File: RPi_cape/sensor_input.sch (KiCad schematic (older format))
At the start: 39 parts, among them U5 LM2903, U6 LMC7101B, U7 LMC7101B

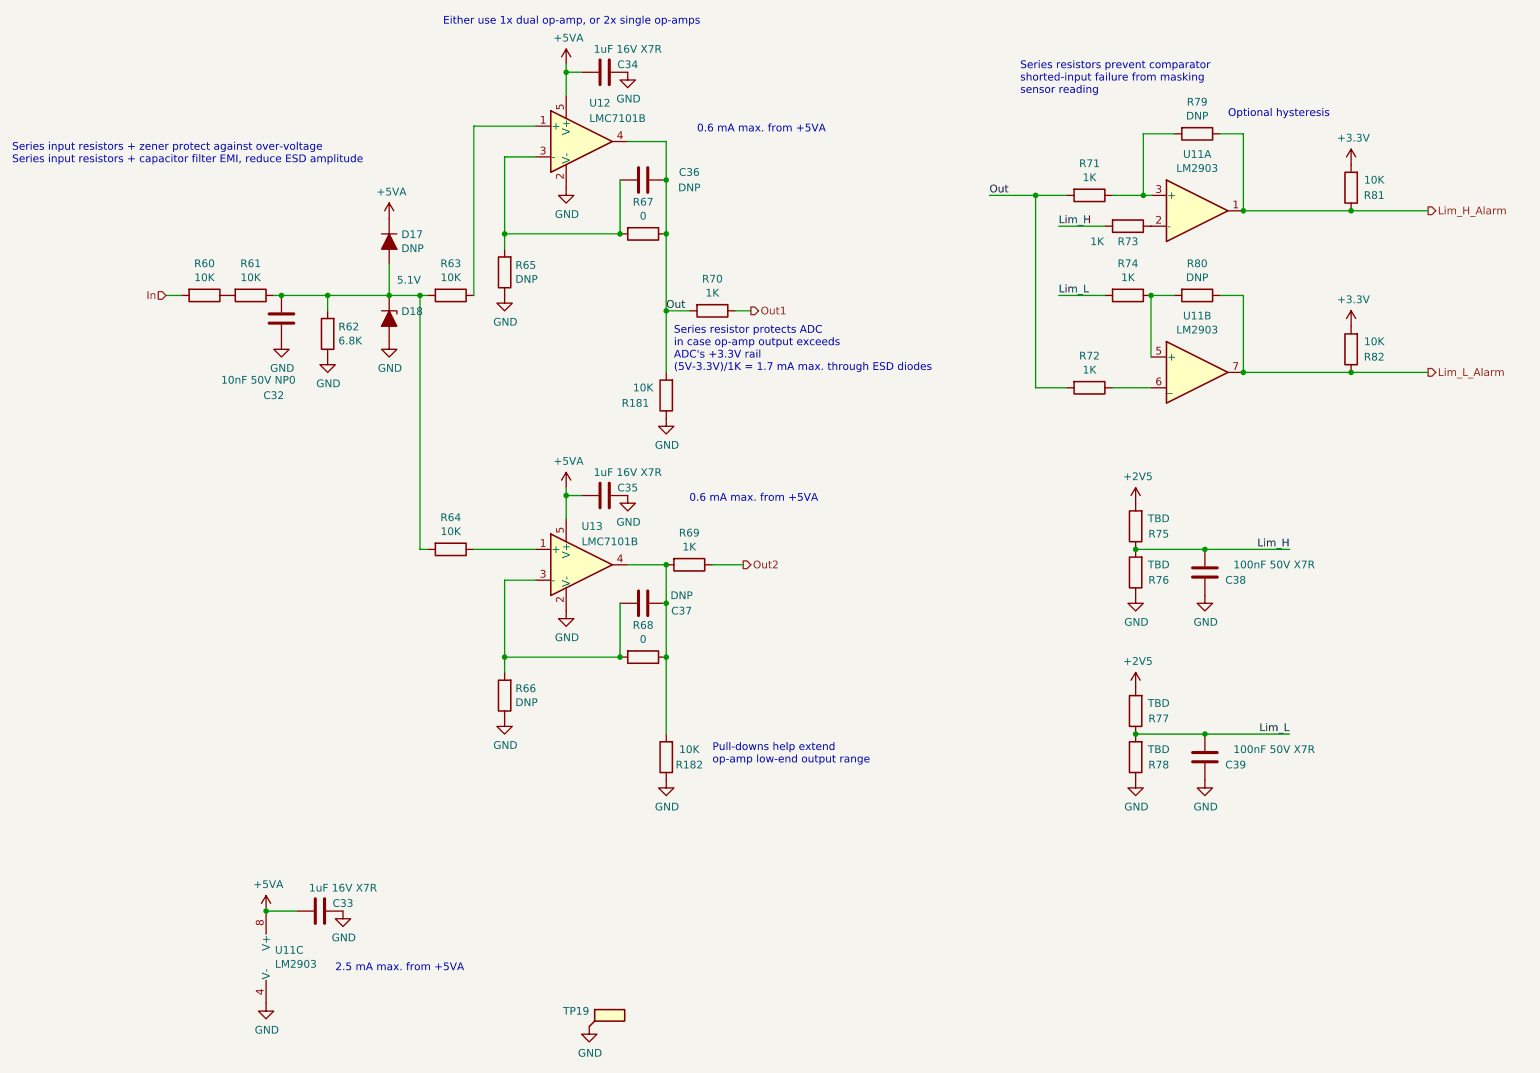
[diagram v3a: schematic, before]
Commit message: Better valve monitoring, finalized layout and manufacturing files
Created assembly and fabrication drawings, assigned all BOM parts, generally made design ready for ordering
Added strain-relief slots and barb mounting dimensions for digital pressure sensors
Changed valve drivers from discrete power MOSFETs to "smart" industrial/automotive driver ICs for the current monitoring, including valve-movement monitor for #4
Connected RPi_Valve* signals to larger CPLD footprint, changed Raspberry Pi pin assignment as a result to ease PCB routing
Updated footprints, page layout to create readable assembly drawing
Added current-measurement testpoints for CPLD power from BATT+
Changed power diodes in power-down-alarm circuit to small-signal parts for more compact layout
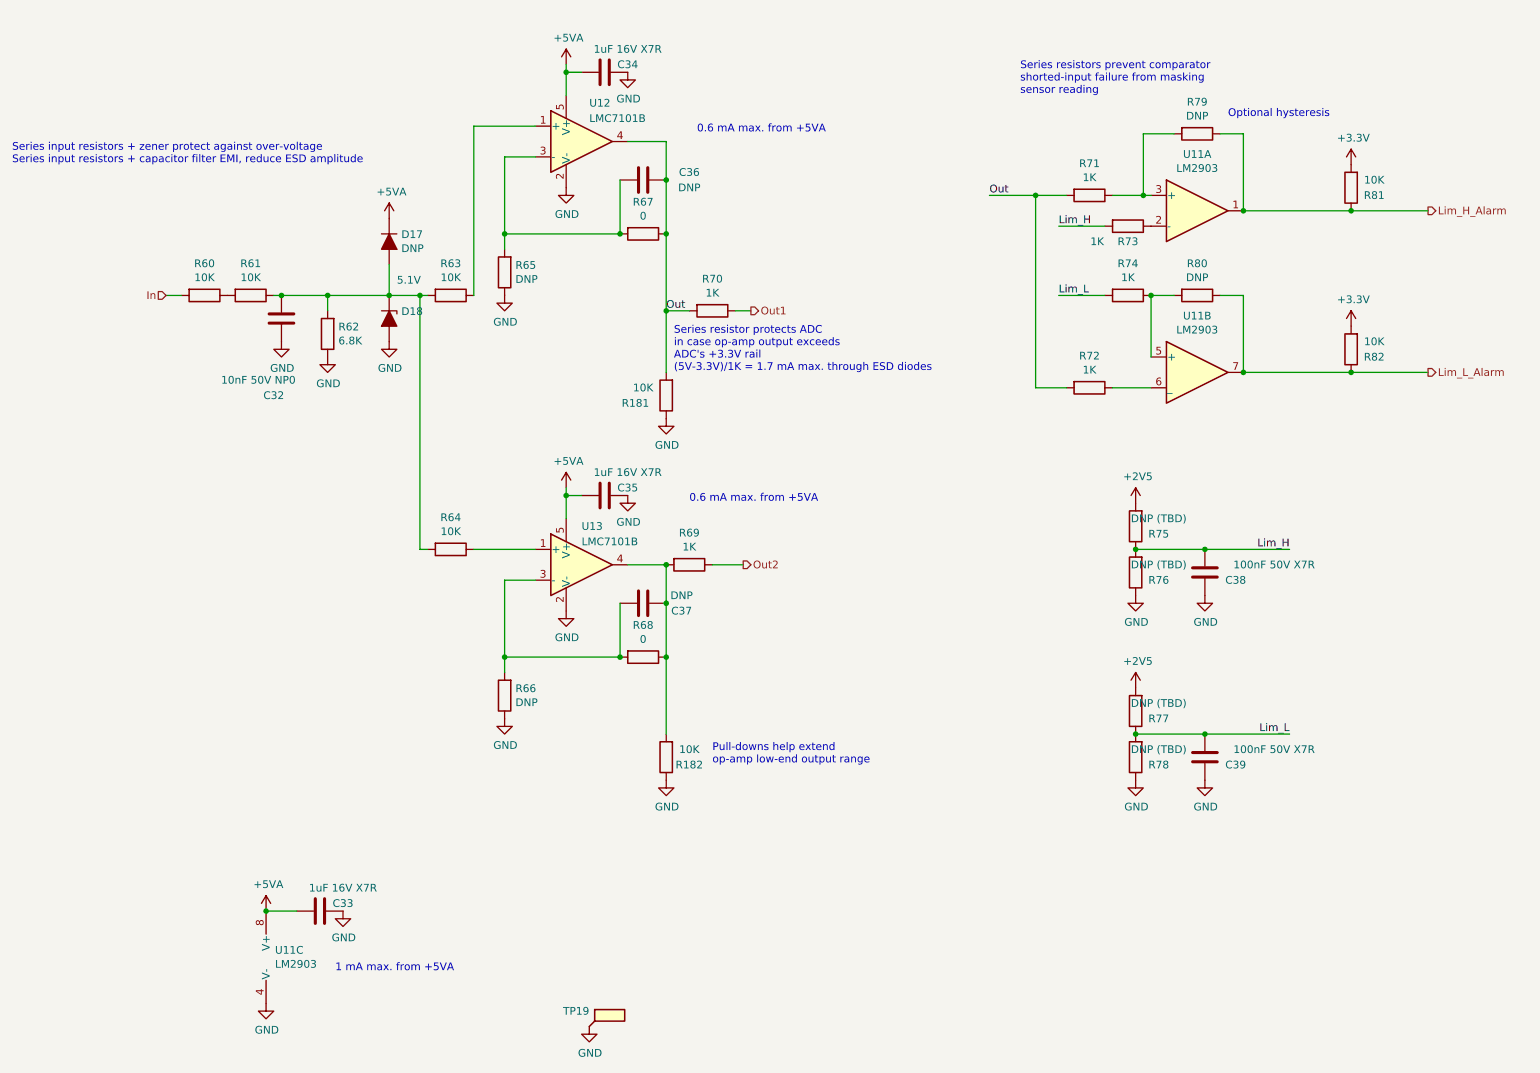
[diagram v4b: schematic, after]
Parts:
- D10: footprint Diode_SMD:D_SOD-123 -> Ventilator:D_SOD-123
- D11: footprint Diode_SMD:D_SOD-123 -> Ventilator:D_SOD-123; Manufacturer (none) -> ON Semiconductor; Part Number (none) -> MMSZ5231BT1G
- R179, R180, R30, R31, R33, R34, R51, R52: Manufacturer (none) -> KOA Speer; Part Number (none) -> RK73H2BTTD1002F
- R32: Manufacturer (none) -> KOA Speer; Part Number (none) -> RK73H2BTTD6801F
- R37, R38: Manufacturer (none) -> Panasonic; Part Number (none) -> ERJ-8GEY0R00V
- R39, R40, R41, R42, R43, R44: Manufacturer (none) -> KOA Speer; Part Number (none) -> RK73H2BTTD1001F
- R45, R46, R47, R48: value TBD -> DNP (TBD)
- U5: footprint Package_SO:VSSOP-8_3.0x3.0mm_P0.65mm -> Ventilator:VSSOP-8_3.0x3.0mm_P0.65mm
- U6, U7: footprint Package_TO_SOT_SMD:SOT-23-5 -> Ventilator:SOT-23-5
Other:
- note added: "1 mA max. from +5VA"
- note removed: "2.5 mA max. from +5VA"
- note removed: "Either use 1x dual op-amp, or 2x single op-amps"
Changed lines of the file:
@@
 $Descr A4 11693 8268
 encoding utf-8
-Sheet 4 14
+Sheet 4 15
 Title "Sensor Input (0-10V)"
 Date ""
@@
 F 2 "Resistor_SMD:R_1206_3216Metric" V 3380 4300 50  0001 C CNN
 F 3 "~" H 3450 4300 50  0001 C CNN
+F 4 "KOA Speer" H 3450 4300 50  0001 C CNN "Manufacturer"
+F 5 "RK73H2BTTD1002F" H 3450 4300 50  0001 C CNN "Part Number"
 	1    3450 4300
 	0    1    1    0
@@
 F 2 "Resistor_SMD:R_1206_3216Metric" V 4630 5000 50  0001 C CNN
 F 3 "~" H 4700 5000 50  0001 C CNN
+F 4 "Panasonic" H 4700 5000 50  0001 C CNN "Manufacturer"
+F 5 "ERJ-8GEY0R00V" H 4700 5000 50  0001 C CNN "Part Number"
 	1    4700 5000
 	0    1    1    0
@@
 F 0 "D18" V 3004 2879 50  0000 L CNN
 F 1 "5.1V" V 2800 2850 50  0000 L CNN
-F 2 "Diode_SMD:D_SOD-123" H 3050 2800 50  0001 C CNN
+F 2 "Ventilator:D_SOD-123" H 3050 2800 50  0001 C CNN
 F 3 "~" H 3050 2800 50  0001 C CNN
+F 4 "ON Semiconductor" H 3050 2800 50  0001 C CNN "Manufacturer"
+F 5 "MMSZ5231BT1G" H 3050 2800 50  0001 C CNN "Part Number"
 	1    3050 2800
 	0    1    1    0
@@
 F 2 "Resistor_SMD:R_1206_3216Metric" V 2580 2900 50  0001 C CNN
 F 3 "~" H 2650 2900 50  0001 C CNN
+F 4 "KOA Speer" H 2650 2900 50  0001 C CNN "Manufacturer"
+F 5 "RK73H2BTTD6801F" H 2650 2900 50  0001 C CNN "Part Number"
 	1    2650 2900
 	-1   0    0    1
@@
 F 2 "Resistor_SMD:R_1206_3216Metric" V 3380 2650 50  0001 C CNN
 F 3 "~" H 3450 2650 50  0001 C CNN
+F 4 "KOA Speer" H 3450 2650 50  0001 C CNN "Manufacturer"
+F 5 "RK73H2BTTD1002F" H 3450 2650 50  0001 C CNN "Part Number"
 	1    3450 2650
 	0    1    1    0
@@
 F 2 "Resistor_SMD:R_1206_3216Metric" V 1780 2650 50  0001 C CNN
 F 3 "~" H 1850 2650 50  0001 C CNN
+F 4 "KOA Speer" H 1850 2650 50  0001 C CNN "Manufacturer"
+F 5 "RK73H2BTTD1002F" H 1850 2650 50  0001 C CNN "Part Number"
 	1    1850 2650
 	0    1    1    0
@@
 F 2 "Resistor_SMD:R_1206_3216Metric" V 2080 2650 50  0001 C CNN
 F 3 "~" H 2150 2650 50  0001 C CNN
+F 4 "KOA Speer" H 2150 2650 50  0001 C CNN "Manufacturer"
+F 5 "RK73H2BTTD1002F" H 2150 2650 50  0001 C CNN "Part Number"
 	1    2150 2650
 	0    1    1    0
@@
 F 2 "Resistor_SMD:R_1206_3216Metric" V 4630 2250 50  0001 C CNN
 F 3 "~" H 4700 2250 50  0001 C CNN
+F 4 "Panasonic" H 4700 2250 50  0001 C CNN "Manufacturer"
+F 5 "ERJ-8GEY0R00V" H 4700 2250 50  0001 C CNN "Part Number"
 	1    4700 2250
 	0    1    1    0
@@
 F 0 "U13" H 4300 4650 50  0000 L CNN
 F 1 "LMC7101B" H 4300 4550 50  0000 L CNN
-F 2 "Package_TO_SOT_SMD:SOT-23-5" H 4300 4400 50  0001 L CNN
+F 2 "Ventilator:SOT-23-5" H 4300 4400 50  0001 L CNN
 F 3 "" H 4300 4400 50  0001 C CNN
 F 4 "Texas Instruments" H 4300 4400 50  0001 C CNN "Manufacturer"
@@
 F 0 "U12" H 4350 1900 50  0000 L CNN
 F 1 "LMC7101B" H 4350 1800 50  0000 L CNN
-F 2 "Package_TO_SOT_SMD:SOT-23-5" H 4300 1650 50  0001 L CNN
+F 2 "Ventilator:SOT-23-5" H 4300 1650 50  0001 L CNN
 F 3 "" H 4300 1650 50  0001 C CNN
 F 4 "Texas Instruments" H 4300 1650 50  0001 C CNN "Manufacturer"
@@
 F 2 "Resistor_SMD:R_1206_3216Metric" V 4930 4400 50  0001 C CNN
 F 3 "~" H 5000 4400 50  0001 C CNN
+F 4 "KOA Speer" H 5000 4400 50  0001 C CNN "Manufacturer"
+F 5 "RK73H2BTTD1001F" H 5000 4400 50  0001 C CNN "Part Number"
 	1    5000 4400
 	0    1    1    0
@@
 F 0 "D17" V 3004 2379 50  0000 L CNN
 F 1 "DNP" V 3095 2379 50  0000 L CNN
-F 2 "Diode_SMD:D_SOD-123" H 3050 2300 50  0001 C CNN
+F 2 "Ventilator:D_SOD-123" H 3050 2300 50  0001 C CNN
 F 3 "~" H 3050 2300 50  0001 C CNN
 	1    3050 2300
@@
 F 0 "U11" H 8300 2467 50  0000 C CNN
 F 1 "LM2903" H 8300 2376 50  0000 C CNN
-F 2 "Package_SO:VSSOP-8_3.0x3.0mm_P0.65mm" H 8300 2100 50  0001 C CNN
+F 2 "Ventilator:VSSOP-8_3.0x3.0mm_P0.65mm" H 8300 2100 50  0001 C CNN
 F 3 "http://www.ti.com/lit/ds/symlink/lm393-n.pdf" H 8300 2100 50  0001 C CNN
 F 4 "Texas Instruments" H 8300 2100 50  0001 C CNN "Manufacturer"
@@
 F 0 "U11" H 8300 3517 50  0000 C CNN
 F 1 "LM2903" H 8300 3426 50  0000 C CNN
-F 2 "Package_SO:VSSOP-8_3.0x3.0mm_P0.65mm" H 8300 3150 50  0001 C CNN
+F 2 "Ventilator:VSSOP-8_3.0x3.0mm_P0.65mm" H 8300 3150 50  0001 C CNN
 F 3 "http://www.ti.com/lit/ds/symlink/lm393-n.pdf" H 8300 3150 50  0001 C CNN
 F 4 "Texas Instruments" H 8300 3150 50  0001 C CNN "Manufacturer"
@@
 F 0 "U11" H 2308 6996 50  0000 L CNN
 F 1 "LM2903" H 2308 6905 50  0000 L CNN
-F 2 "Package_SO:VSSOP-8_3.0x3.0mm_P0.65mm" H 2350 6950 50  0001 C CNN
+F 2 "Ventilator:VSSOP-8_3.0x3.0mm_P0.65mm" H 2350 6950 50  0001 C CNN
 F 3 "http://www.ti.com/lit/ds/symlink/lm393-n.pdf" H 2350 6950 50  0001 C CNN
 F 4 "Texas Instruments" H 2350 6950 50  0001 C CNN "Manufacturer"
@@
 F 2 "Resistor_SMD:R_1206_3216Metric" V 5080 2750 50  0001 C CNN
 F 3 "~" H 5150 2750 50  0001 C CNN
+F 4 "KOA Speer" H 5150 2750 50  0001 C CNN "Manufacturer"
+F 5 "RK73H2BTTD1001F" H 5150 2750 50  0001 C CNN "Part Number"
 	1    5150 2750
 	0    1    1    0
@@
 F 2 "Resistor_SMD:R_1206_3216Metric" V 7530 2000 50  0001 C CNN
 F 3 "~" H 7600 2000 50  0001 C CNN
+F 4 "KOA Speer" H 7600 2000 50  0001 C CNN "Manufacturer"
+F 5 "RK73H2BTTD1001F" H 7600 2000 50  0001 C CNN "Part Number"
 	1    7600 2000
 	0    1    1    0
@@
 F 2 "Resistor_SMD:R_1206_3216Metric" V 7530 3250 50  0001 C CNN
 F 3 "~" H 7600 3250 50  0001 C CNN
+F 4 "KOA Speer" H 7600 3250 50  0001 C CNN "Manufacturer"
+F 5 "RK73H2BTTD1001F" H 7600 3250 50  0001 C CNN "Part Number"
 	1    7600 3250
 	0    1    1    0
@@
 F 2 "Resistor_SMD:R_1206_3216Metric" V 9230 1950 50  0001 C CNN
 F 3 "~" H 9300 1950 50  0001 C CNN
+F 4 "KOA Speer" H 9300 1950 50  0001 C CNN "Manufacturer"
+F 5 "RK73H2BTTD1002F" H 9300 1950 50  0001 C CNN "Part Number"
 	1    9300 1950
 	-1   0    0    1
@@
 AR Path="/5E8A4ABF/5EC162C6" Ref="R75"  Part="1"
 F 0 "R75" H 7750 4200 50  0000 C CNN
-F 1 "TBD" H 7750 4100 50  0000 C CNN
+F 1 "DNP (TBD)" H 7750 4100 50  0000 C CNN
 F 2 "Resistor_SMD:R_1206_3216Metric" V 7830 4150 50  0001 C CNN
 F 3 "~" H 7900 4150 50  0001 C CNN
@@
 AR Path="/5E8A4ABF/5EC16810" Ref="R76"  Part="1"
 F 0 "R76" H 7750 4500 50  0000 C CNN
-F 1 "TBD" H 7750 4400 50  0000 C CNN
+F 1 "DNP (TBD)" H 7750 4400 50  0000 C CNN
 F 2 "Resistor_SMD:R_1206_3216Metric" V 7830 4450 50  0001 C CNN
 F 3 "~" H 7900 4450 50  0001 C CNN
@@
 AR Path="/5E8A4ABF/5EC2DDB8" Ref="R77"  Part="1"
 F 0 "R77" H 7750 5400 50  0000 C CNN
-F 1 "TBD" H 7750 5300 50  0000 C CNN
+F 1 "DNP (TBD)" H 7750 5300 50  0000 C CNN
 F 2 "Resistor_SMD:R_1206_3216Metric" V 7830 5350 50  0001 C CNN
 F 3 "~" H 7900 5350 50  0001 C CNN
@@
 AR Path="/5E8A4ABF/5EC2DDBE" Ref="R78"  Part="1"
 F 0 "R78" H 7750 5700 50  0000 C CNN
-F 1 "TBD" H 7750 5600 50  0000 C CNN
+F 1 "DNP (TBD)" H 7750 5600 50  0000 C CNN
 F 2 "Resistor_SMD:R_1206_3216Metric" V 7830 5650 50  0001 C CNN
 F 3 "~" H 7900 5650 50  0001 C CNN
@@
 F 2 "Resistor_SMD:R_1206_3216Metric" V 7780 2650 50  0001 C CNN
 F 3 "~" H 7850 2650 50  0001 C CNN
+F 4 "KOA Speer" H 7850 2650 50  0001 C CNN "Manufacturer"
+F 5 "RK73H2BTTD1001F" H 7850 2650 50  0001 C CNN "Part Number"
 	1    7850 2650
 	0    1    1    0
@@
 F 2 "Resistor_SMD:R_1206_3216Metric" V 7780 2200 50  0001 C CNN
 F 3 "~" H 7850 2200 50  0001 C CNN
+F 4 "KOA Speer" H 7850 2200 50  0001 C CNN "Manufacturer"
+F 5 "RK73H2BTTD1001F" H 7850 2200 50  0001 C CNN "Part Number"
 	1    7850 2200
 	0    1    1    0
@@
 	7700 2200 7400 2200
 Text Notes 2700 7050 0    50   ~ 0
-2.5 mA max. from +5VA
+1 mA max. from +5VA
 Text Notes 5050 1600 0    50   ~ 0
 0.6 mA max. from +5VA
@@
 F 2 "Resistor_SMD:R_1206_3216Metric" V 9230 3000 50  0001 C CNN
 F 3 "~" H 9300 3000 50  0001 C CNN
+F 4 "KOA Speer" H 9300 3000 50  0001 C CNN "Manufacturer"
+F 5 "RK73H2BTTD1002F" H 9300 3000 50  0001 C CNN "Part Number"
 	1    9300 3000
 	-1   0    0    1
@@
 Text Notes 600  1800 0    50   ~ 0
 Series input resistors + zener protect against over-voltage\nSeries input resistors + capacitor filter EMI, reduce ESD amplitude
-Text Notes 3400 900  0    50   ~ 0
-Either use 1x dual op-amp, or 2x single op-amps
 $Comp
 L Device:R R?
@@
 F 2 "Resistor_SMD:R_1206_3216Metric" V 4780 5650 50  0001 C CNN
 F 3 "~" H 4850 5650 50  0001 C CNN
+F 4 "KOA Speer" H 4850 5650 50  0001 C CNN "Manufacturer"
+F 5 "RK73H2BTTD1002F" H 4850 5650 50  0001 C CNN "Part Number"
 	1    4850 5650
 	-1   0    0    1
@@
 F 2 "Resistor_SMD:R_1206_3216Metric" V 4780 3300 50  0001 C CNN
 F 3 "~" H 4850 3300 50  0001 C CNN
+F 4 "KOA Speer" H 4850 3300 50  0001 C CNN "Manufacturer"
+F 5 "RK73H2BTTD1002F" H 4850 3300 50  0001 C CNN "Part Number"
 	1    4850 3300
 	-1   0    0    1

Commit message: Manufacturing clean-up
Corrections and additions to BOM etc. for manufacturing
Added power draw tracking spreadsheet
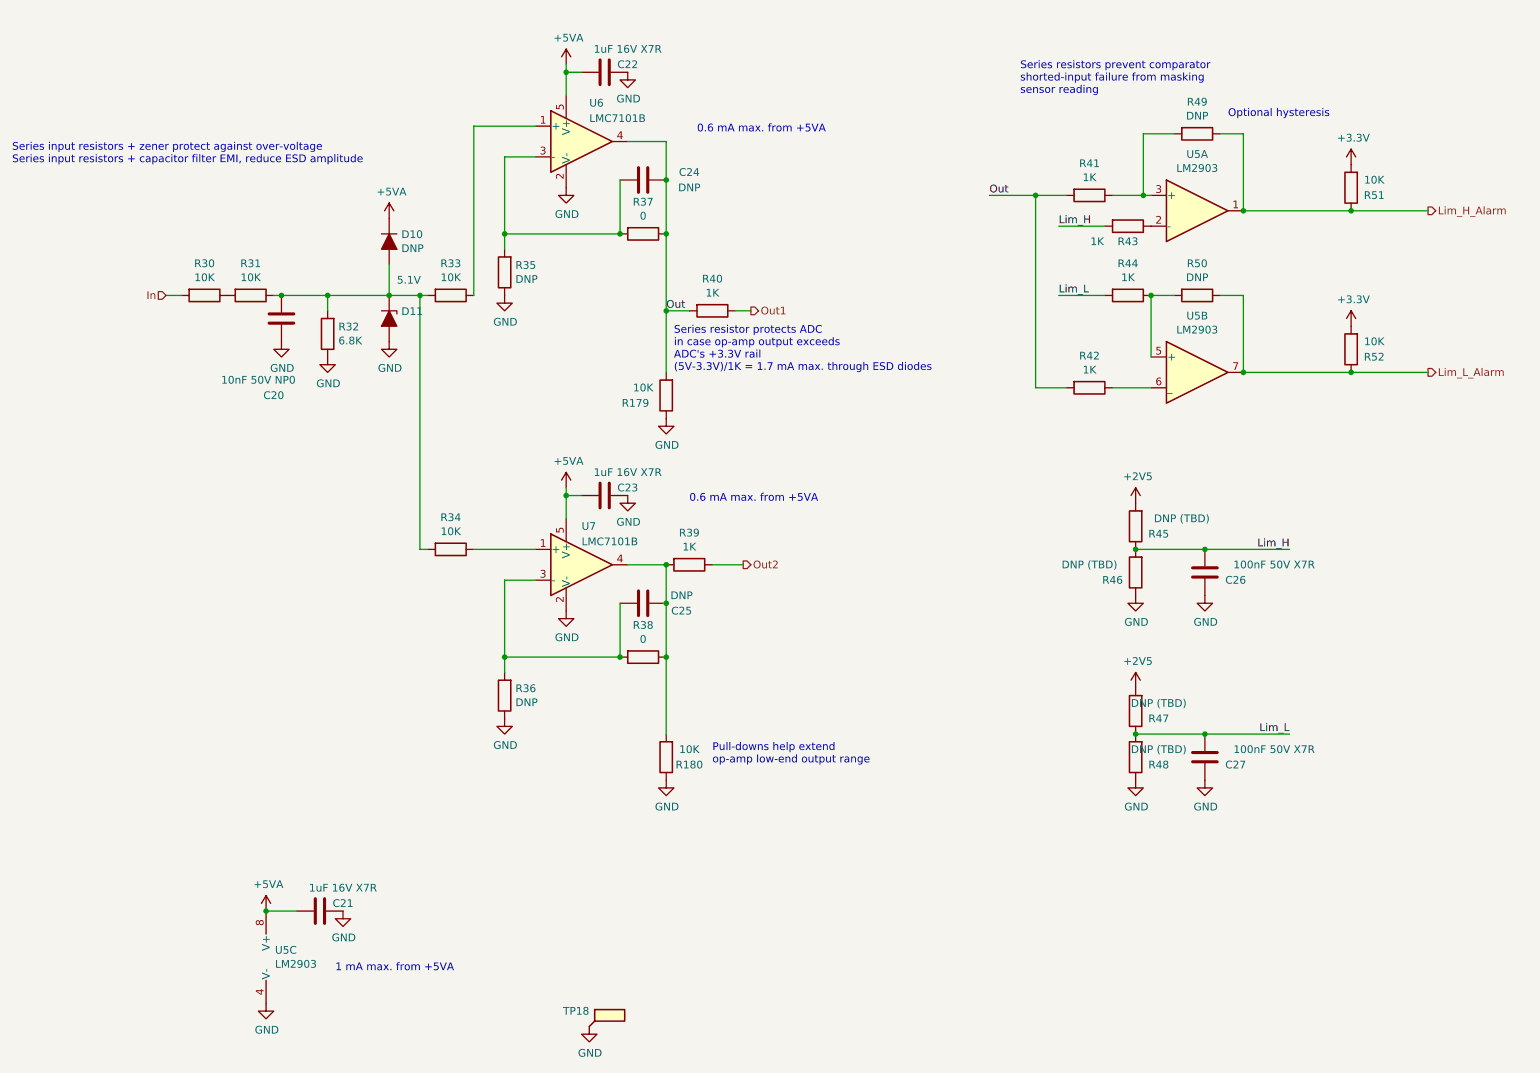
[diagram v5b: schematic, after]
